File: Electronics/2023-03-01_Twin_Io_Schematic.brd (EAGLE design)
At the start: 160 x 100 mm, 152 parts, among them IC1 7805, IC2 LD1117S33, U1 INA317IDGKT, U10 INA317IDGKT, U11 INA317IDGKT, U12 INA317IDGKT, U13 ADS131A04IPBSR, U14 ADS131A04IPBSR, U15 ADS131A04IPBSR, U16 OPA325IDBVR, U17 STM32F105R8T6, U2 INA317IDGKT, U3 INA317IDGKT, U4 INA317IDGKT, U5 INA317IDGKT, U6 INA317IDGKT, U7 INA317IDGKT, U8 INA317IDGKT, U9 INA317IDGKT, Y1 ABM3C-16.384MHZ-D4Y-T, Y2 ABM3C-16.384MHZ-D4Y-T, Y3 ABM3C-16.384MHZ-D4Y-T

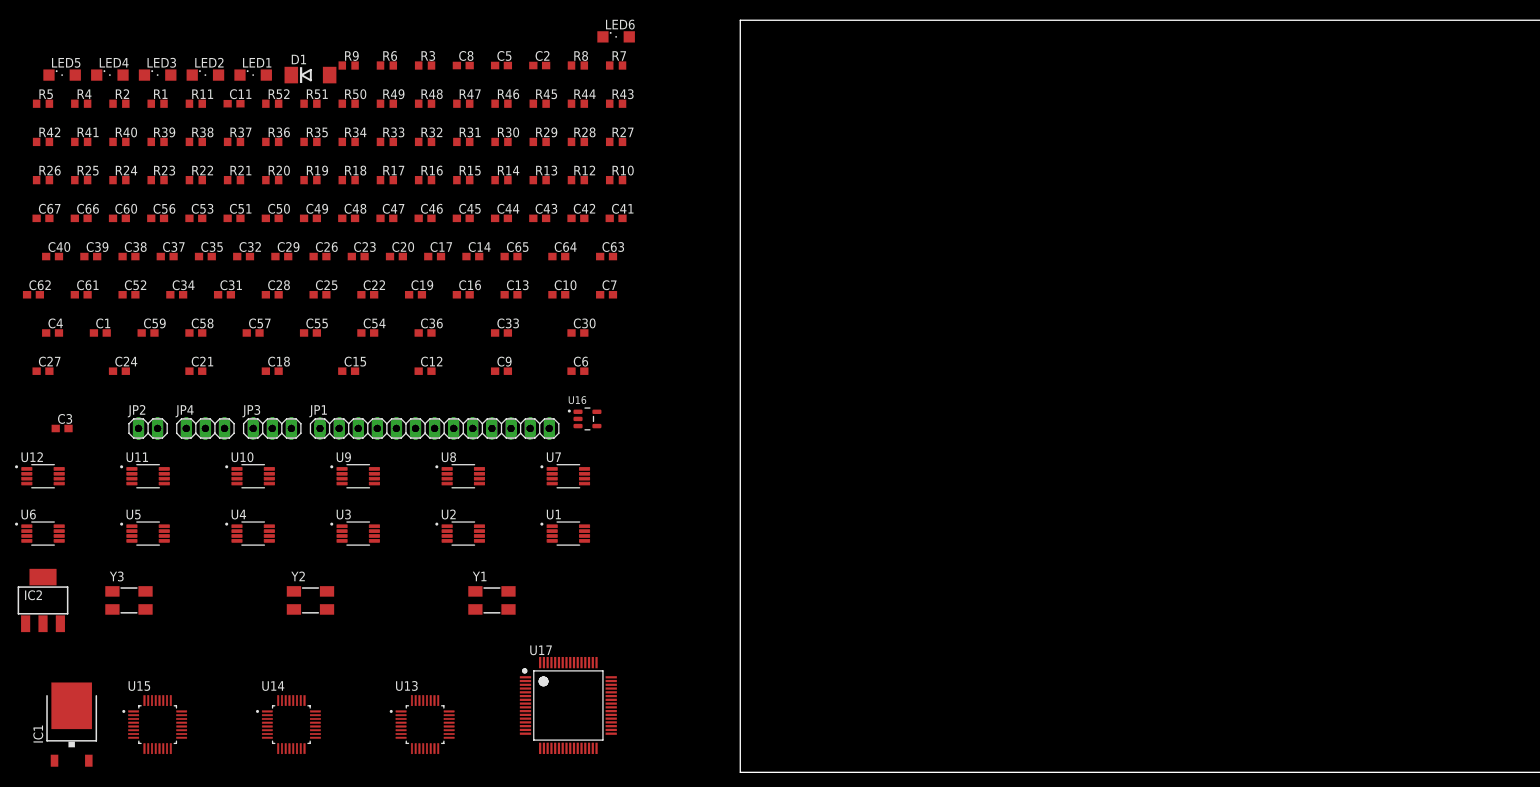
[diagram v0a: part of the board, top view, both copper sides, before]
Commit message: First Prototype Version of Schematic and PCB done
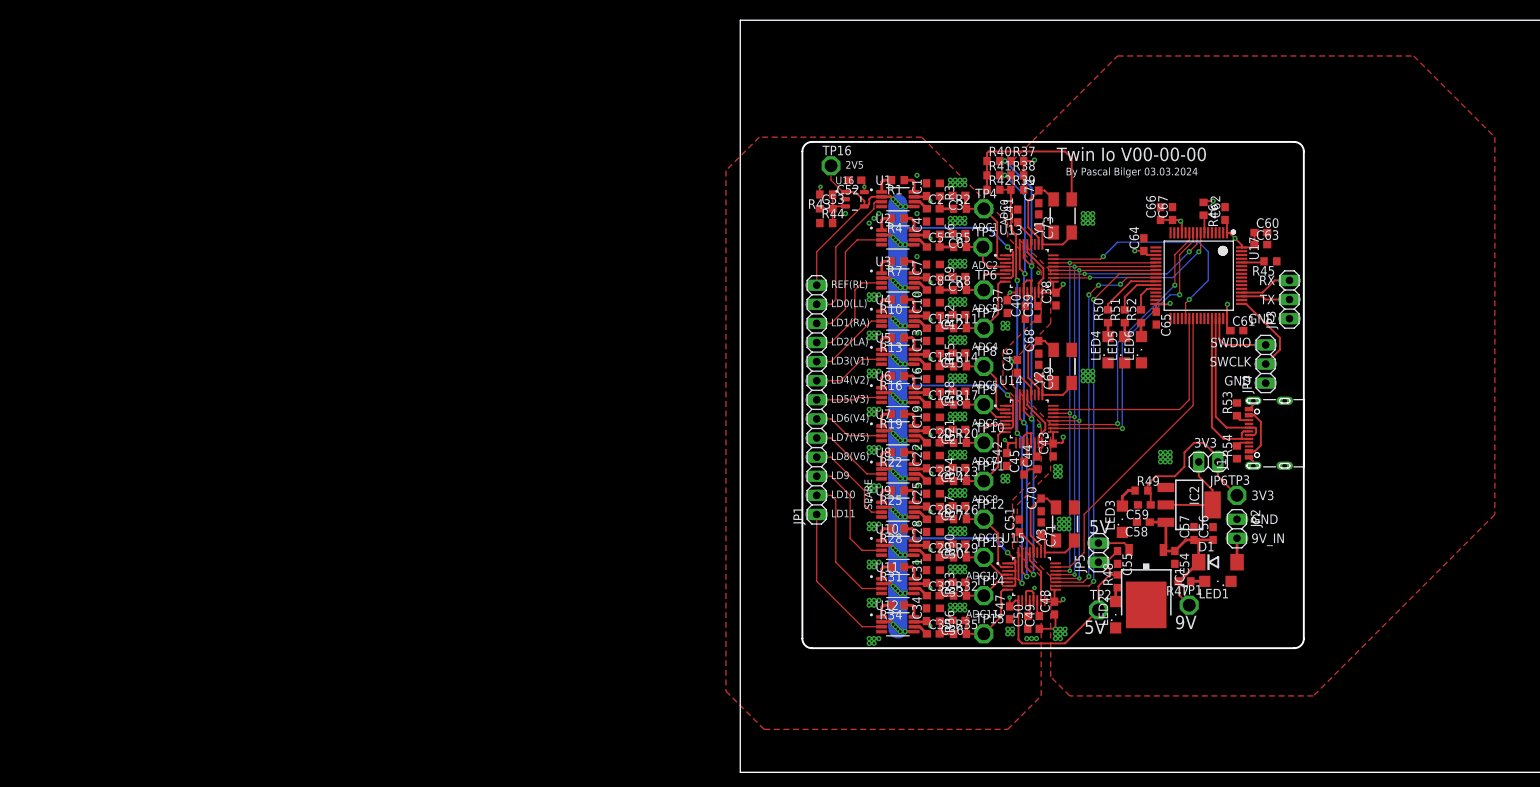
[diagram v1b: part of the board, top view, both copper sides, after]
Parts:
- added C68, C69, C70, C71, C72, C73: 18p, rcl:C0603
- added J1: 12402012E212A, USB-C:AMPHENOL_12402012E212A
- added JP5, JP6: (no value), pinhead:1X02
- added R53, R54: 5k1, rcl:R0603
- added TP1, TP10, TP11, TP12, TP13, TP14, TP15, TP16, TP2, TP3, TP4, TP5, TP6, TP7, TP8, TP9: TPPAD1-17, testpad:P1-17
- moved C62 158.8 mm to (64.5, 74.3), turned to 90 degrees
- moved C61 153.7 mm to (66.0, 58.7)
- moved IC2 152.9 mm to (59.7, 35.6), turned to 270 degrees
- moved C60 151.8 mm to (69.2, 71.8)
- moved C67 150.2 mm to (57.5, 74.3), turned to 90 degrees
- moved C56 146.5 mm to (62.9, 31.8), turned to 90 degrees
- moved LED5 145.9 mm to (51.1, 56.2), turned to 90 degrees
- moved JP2 145.4 mm to (66.0, 32.4), turned to 270 degrees
- moved LED1 144.9 mm to (63.5, 25.4), turned to 180 degrees
- moved IC1 144.1 mm to (54.0, 24.8), turned to 180 degrees
- moved C66 143.5 mm to (55.9, 74.3), turned to 90 degrees
- moved JP4 141.2 mm to (69.8, 54.3), turned to 90 degrees
- moved LED3 141.2 mm to (50.8, 33.7), turned to 90 degrees
- moved LED2 140.7 mm to (49.9, 21.0), turned to 90 degrees
- moved LED4 137.6 mm to (48.9, 56.2), turned to 90 degrees
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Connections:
- removed net ADC_CS: U13.23
- new net MCO: U17.41
- new net N$74: J1.A5, R54.2
- new net N$75: J1.B5, R53.1
- new net N$76: IC1.2, JP5.2
- new net N$78: IC2.2, IC2.4, JP6.2
- new net VBUS: J1.A4_B9, J1.B4_A9
- net 2V5: now also TP16.TP
- net 3V3: now also JP6.1, TP3.TP; no longer C52.1, IC2.2, IC2.4, U16.5
- net 5V: now also C25.1, C28.1, C31.1, C34.1, C52.1, JP5.1, TP2.TP, U16.5; no longer IC1.2
- net 9V: now also TP1.TP
- net ADC0: now also TP4.TP
- net ADC0_CS: now also U13.23
- net ADC1: now also TP5.TP
- net ADC10: now also TP14.TP
- net ADC11: now also TP15.TP
- net ADC2: now also TP6.TP
- net ADC3: now also TP7.TP
- net ADC4: now also TP8.TP
- net ADC5: now also TP9.TP
- net ADC6: now also TP10.TP
- net ADC7: now also TP11.TP
- net ADC8: now also TP12.TP
- net ADC9: now also TP13.TP
- net GND: now also C68.1, C69.1, C70.1, C71.1, C72.1, C73.1, J1.A1_B12, J1.B1_A12, J1.SH1, J1.SH2, J1.SH3, J1.SH4, R53.2, R54.1
- net N$43: now also C69.2
- net N$46: now also C68.2
- net N$48: now also C70.2, U15.26, Y3.3; no longer U15.25, Y3.1
- net N$51: now also C71.2, U15.25, Y3.1; no longer U15.26, Y3.3
- net N$7: now also C72.2
- net N$8: now also C73.2
- net USB+: now also J1.A6, J1.B6
- net USB-: now also J1.A7, J1.B7
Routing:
- net 2V5: track 0.00 -> 211.7 mm, vias 0 -> 63
- net 3V3: track 0.00 -> 90.6 mm, vias 0 -> 10
- net 5V: track 0.00 -> 71.5 mm, vias 0 -> 17
- net ADC_MODE_0: track 0.00 -> 68.4 mm, vias 0 -> 4
- net ADC_MODE_1: track 0.00 -> 67.7 mm, vias 0 -> 4
- net ADC_MODE_2: track 0.00 -> 63.9 mm, vias 0 -> 3
- net ADC_DIN: track 0.00 -> 61.3 mm, vias 0 -> 3
- net ADC_DOUT: track 0.00 -> 60.0 mm, vias 0 -> 3
- net ADC_SCLK: track 0.00 -> 58.7 mm, vias 0 -> 3
- net ADC2_DONE: track 0.00 -> 52.5 mm, vias 0 -> 2
- net ADC2_DRDY: track 0.00 -> 52.1 mm, vias 0 -> 4
- net GND: track 0.00 -> 42.7 mm, vias 0 -> 230
- net ADC2_CS: track 0.00 -> 41.7 mm
- net ADC1_DONE: track 0.00 -> 39.9 mm, vias 0 -> 2
- net ADC1_DRDY: track 0.00 -> 37.9 mm, vias 0 -> 2
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- added copper zone on layer 2, net 3V3
- added copper zone on layer 2, net 5V
- added copper zone on layer 1, net GND
- added copper zone on layer 15, net GND
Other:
- outline, holes or cut-outs redrawn
- board text added: "2V5"
- board text added: "3V3"
- board text added: "5V"
- board text added: "9V"
- board text added: "9V_IN"
- board text added: "ADC0"
- board text added: "ADC1"
- board text added: "ADC10"
- board text added: "ADC11"
- board text added: "ADC2"
- board text added: "ADC3"
- board text added: "ADC4"
- board text added: "ADC5"
- board text added: "ADC6"
- board text added: "ADC7"
- board text added: "ADC8"
- board text added: "ADC9"
- board text added: "By Pascal Bilger 03.03.2024"
- board text added: "GND"
- board text added: "LD0(LL)"
- board text added: "LD1(RA)"
- board text added: "LD10"
- board text added: "LD11"
- board text added: "LD2(LA)"
- board text added: "LD3(V1)"
- board text added: "LD4(V2)"
- board text added: "LD5(V3)"
- board text added: "LD6(V4)"
- board text added: "LD7(V5)"
- board text added: "LD8(V6)"
- board text added: "LD9"
- board text added: "REF(RL)"
- board text added: "RX"
- board text added: "SPARE"
- board text added: "SWCLK"
- board text added: "SWDIO"
- board text added: "TX"
- board text added: "Twin Io V00-00-00"
